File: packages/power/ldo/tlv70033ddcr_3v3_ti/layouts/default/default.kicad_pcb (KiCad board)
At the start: 2 copper layers, 3 parts

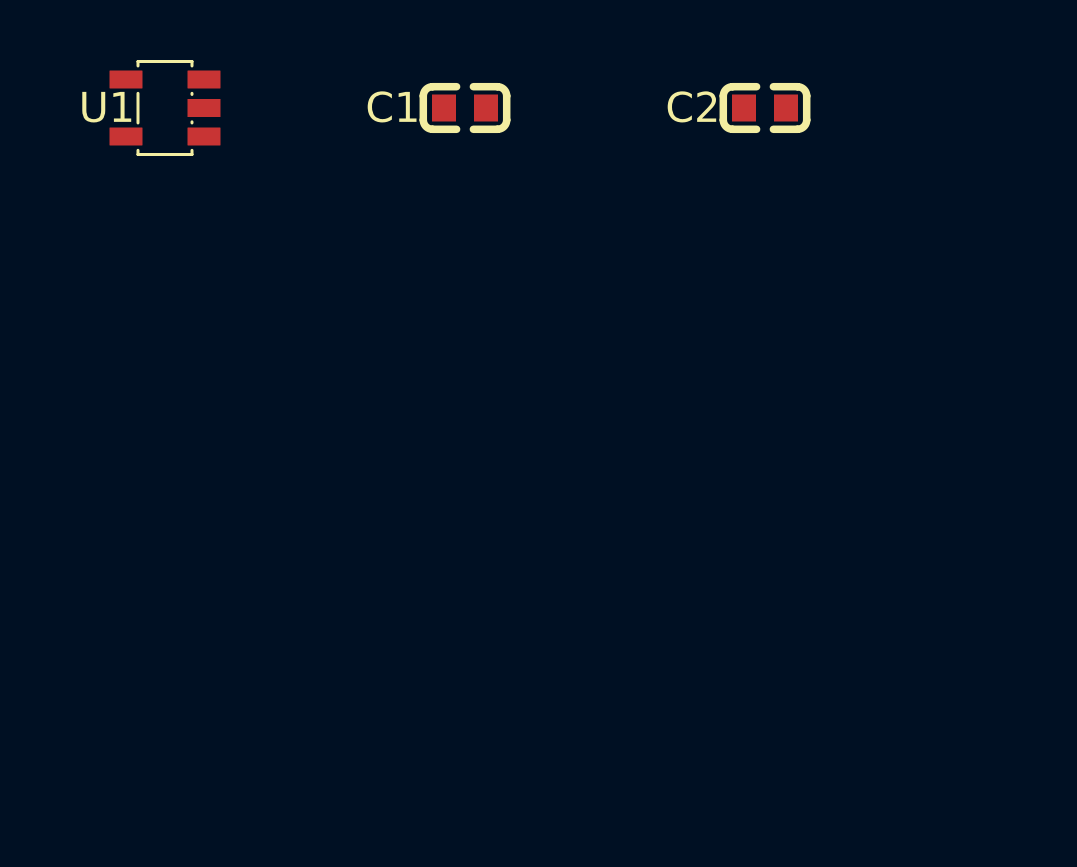
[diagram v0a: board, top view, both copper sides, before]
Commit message: TLV70033 update
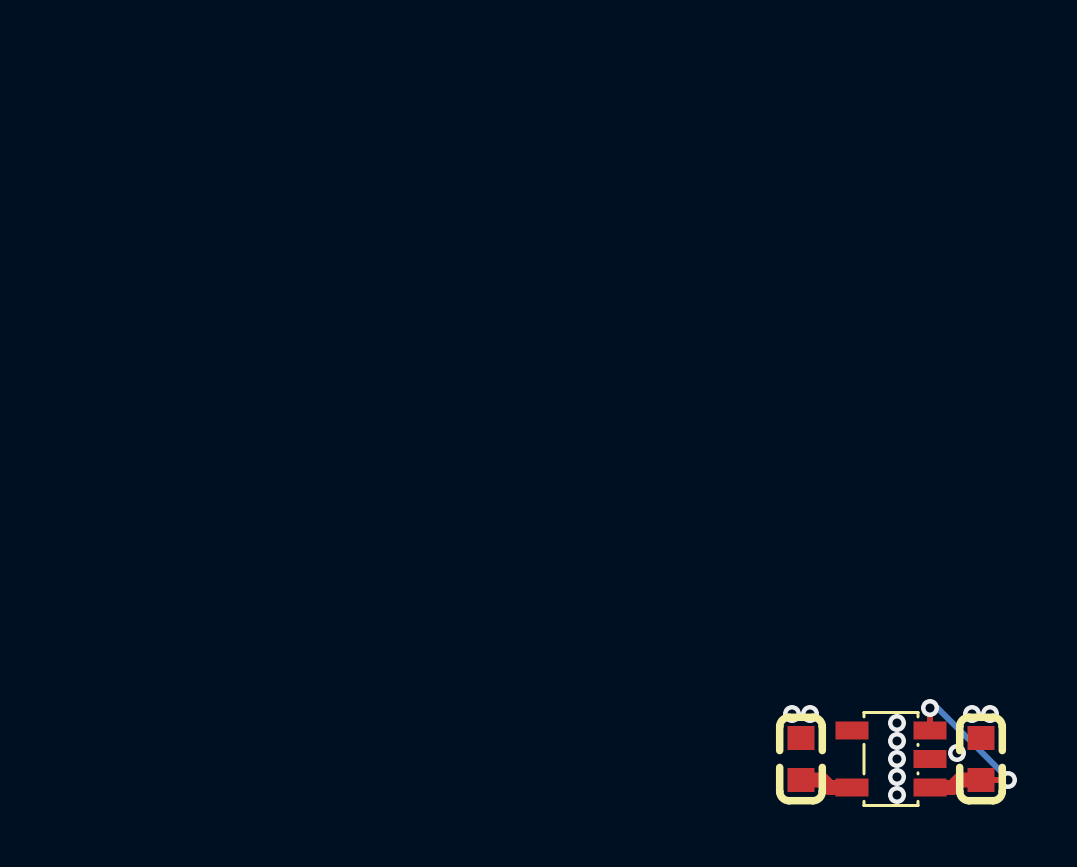
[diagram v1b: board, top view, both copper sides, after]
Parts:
- moved U1 32.5 mm to (24.2, 21.7)
- moved C1 27.7 mm to (27.2, 21.7), turned to 90 degrees
- moved C2 21.7 mm to (21.2, 21.7), turned to 90 degrees
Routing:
- net hv: track 0.00 -> 7.28 mm, vias 0 -> 2
- net power_out-hv: track 0.00 -> 1.80 mm
- net lv: vias 0 -> 10
